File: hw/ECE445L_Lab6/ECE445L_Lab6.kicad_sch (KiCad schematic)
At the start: 32 parts, among them J1 JTAG, J2 Battery, SW1 Reset, SW2 Input, U1 TM4C123GH6PMIR, U2 Adafruit ST7735R, U3 LP2950-33LPRE3, Y1 ABM3-16.000MHZ-B2-T

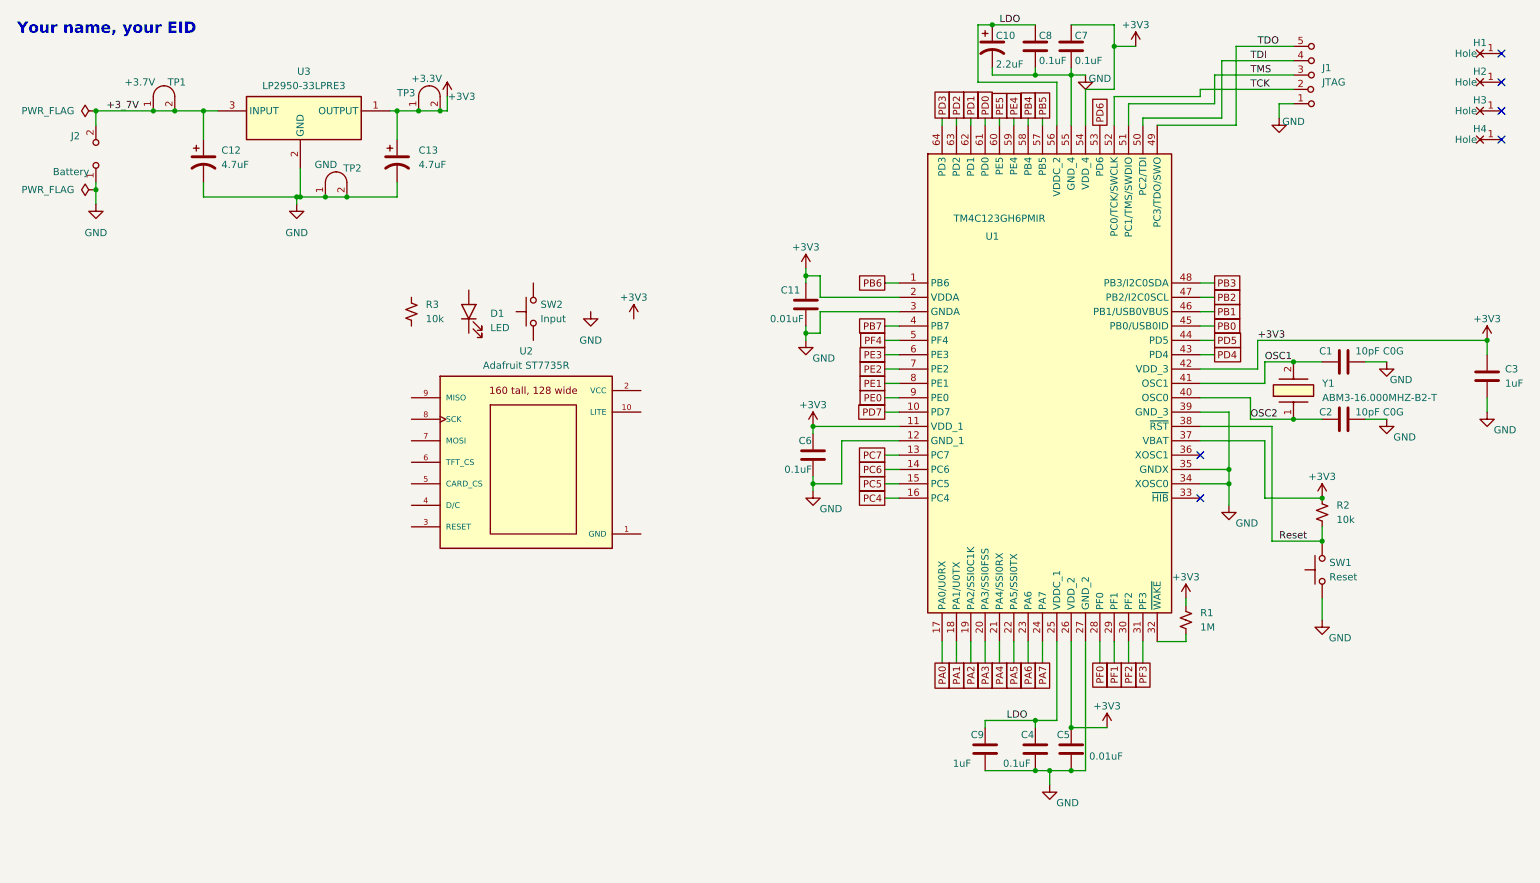
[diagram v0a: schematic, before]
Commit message: all hardware changes
fully updated schematic and pcb, most of changes were local to prevent corrupting files when pulling.
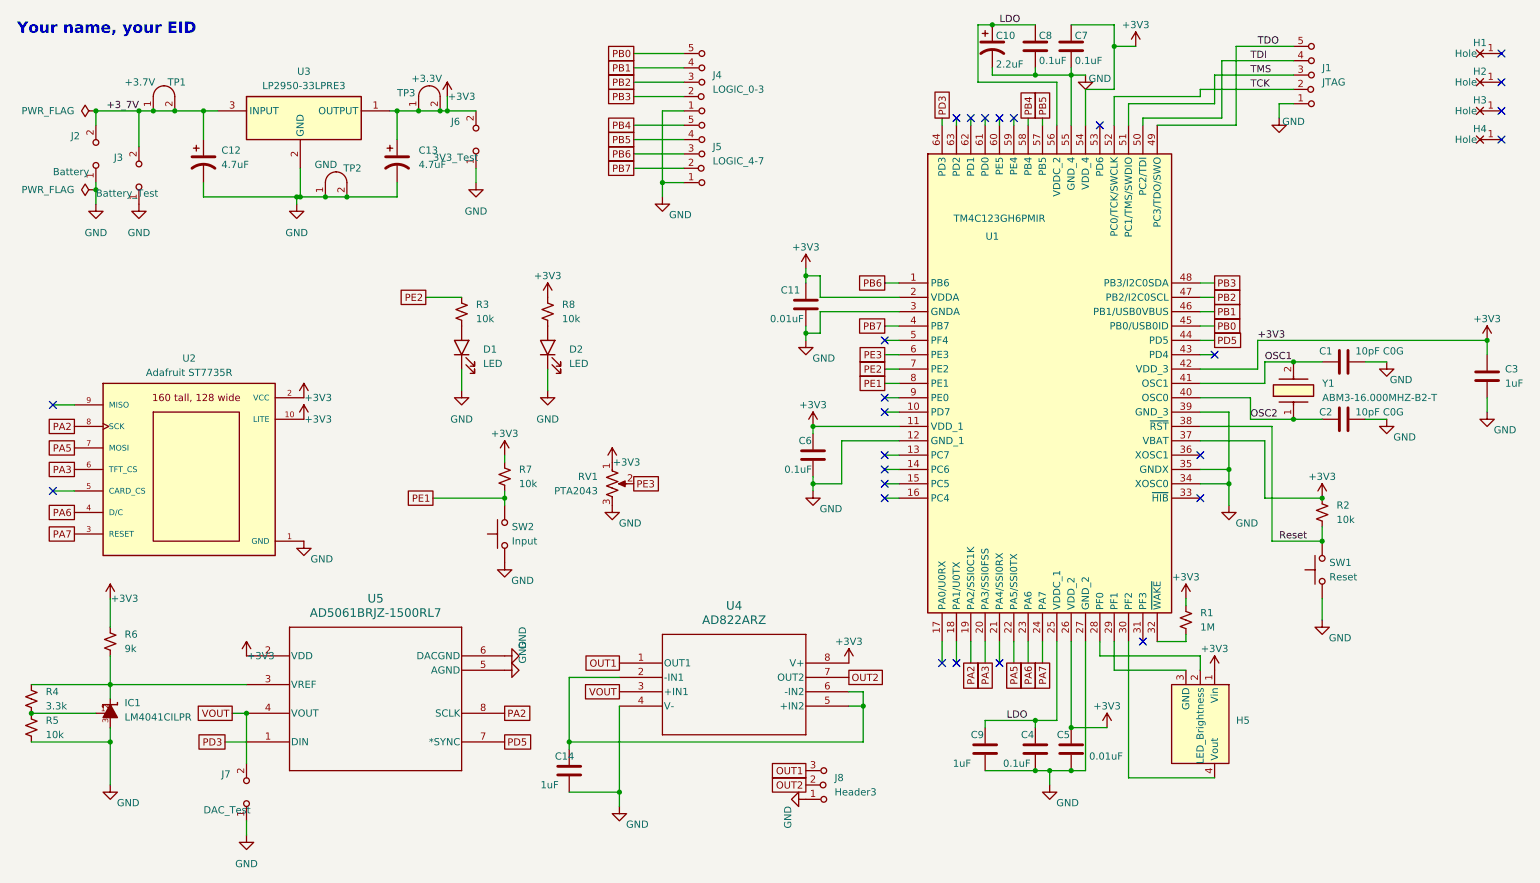
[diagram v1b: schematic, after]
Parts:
- added C14: 1uF, ECE445L:C_Axial_200mil, symbol ECE445L:C
- added D2: LED, ECE445L:LED_D5.0mm, symbol ECE445L:LED
- added H5: ~, Lab_6:HEARTBEAT, symbol lab6:heartbeat
- added IC1: LM4041CILPR, ECE445L:ti_LM4041CILPR, symbol ECE445L:LM4041CILPR
- added J3: Battery_Test, ECE445L:PinHeader_1x02_P2.54mm_Vertical, symbol ECE445L:Header_2
- added J4: LOGIC_0-3, ECE445L:PinHeader_1x05_P2.54mm_Vertical, symbol ECE445L:Header_5
- added J5: LOGIC_4-7, ECE445L:PinHeader_1x05_P2.54mm_Vertical, symbol ECE445L:Header_5
- added J6: 3V3_Test, ECE445L:PinHeader_1x02_P2.54mm_Vertical, symbol ECE445L:Header_2
- added J7: DAC_Test, ECE445L:PinHeader_1x02_P2.54mm_Vertical, symbol ECE445L:Header_2
- added J8: Header3, ECE445L:PinHeader_1x03_P2.54mm_Vertical, symbol ECE445L:Header_3
- added R4: 3.3k, ECE445L:R_Axial_DIN0204_L3.6mm_D1.6mm_P7.62mm_Horizontal, symbol ECE445L:R_0.125W
- added R5, R7, R8: 10k, ECE445L:R_Axial_DIN0204_L3.6mm_D1.6mm_P7.62mm_Horizontal, symbol ECE445L:R_0.125W
- added R6: 9k, ECE445L:R_Axial_DIN0204_L3.6mm_D1.6mm_P7.62mm_Horizontal, symbol ECE445L:R_0.125W
- added RV1: PTA2043, ECE445L:PTA2043pot, symbol ECE445L:PTA2043pot
- added U4: AD822ARZ, Lab_6:R_8_ADI, symbol AD822ARZ:AD822ARZ
- added U5: AD5061BRJZ-1500RL7, Lab_6:RJ_8_ADI, symbol AD5061BRJZ_1500RL7:AD5061BRJZ-1500RL7
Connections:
- net +3V3: now also U2.10 (LITE), U2.2 (VCC), H5.1 (Vin), J6.2 (B), R6.1, R7.1, R8.1, RV1.1, U4.8 (V+), U5.2 (VDD)
- net +3_7V: now also J3.2 (B)
- net GND: now also D1.1 (K), SW2.1, U2.1 (GND), C14.2, D2.1 (K), IC1.3, J3.1 (A), J4.1 (A), J5.1 (A), J6.1 (A), J7.1 (A), J8.1 (A), R5.2, RV1.3, U4.4 (V-), U5.5 (AGND), U5.6 (DACGND)
- net PA2: now also U2.8 (SCK), U5.8 (SCLK)
- net PA3: now also U2.6 (TFT_CS)
- net PA5: now also U2.7 (MOSI)
- net PA6: now also U2.4 (D/C)
- net PA7: now also U2.3 (RESET)
- net PB0: now also J4.5 (C)
- net PB1: now also J4.4 (C)
- net PB2: now also J4.3 (C)
- net PB3: now also J4.2 (B)
- net PB4: now also J5.5 (C)
- net PB5: now also J5.4 (C)
- net PB6: now also J5.3 (C)
- net PB7: now also J5.2 (B)
- net PD3: now also U5.1 (DIN)
- net PD5: now also U5.7 (*SYNC)
- net PE1: now also SW2.2, R7.2
- net PE2: now also R3.1
- net PE3: now also RV1.2
- net at D1.2 (A): now also R3.2
- net PA0: no longer names the net of U1.17 (PA0/U0RX)
- net PA1: no longer names the net of U1.18 (PA1/U0TX)
- net PA4: no longer names the net of U1.21 (PA4/SSI0RX)
- net PC4: no longer names the net of U1.16 (PC4)
- net PC5: no longer names the net of U1.15 (PC5)
- net PC6: no longer names the net of U1.14 (PC6)
- net PC7: no longer names the net of U1.13 (PC7)
- net PD0: no longer names the net of U1.61 (PD0)
- net PD1: no longer names the net of U1.62 (PD1)
- net PD2: no longer names the net of U1.63 (PD2)
- net PD4: no longer names the net of U1.43 (PD4)
- net PD6: no longer names the net of U1.53 (PD6)
- net PD7: no longer names the net of U1.10 (PD7)
- net PE0: no longer names the net of U1.9 (PE0)
- net PE4: no longer names the net of U1.59 (PE4)
- net PE5: no longer names the net of U1.60 (PE5)
- net PF0: no longer names the net of U1.28 (PF0)
- net PF0: now also H5.2 (LED_Brightness)
- net PF1: no longer names the net of U1.29 (PF1)
- net PF1: now also H5.3 (GND)
- net PF2: no longer names the net of U1.30 (PF2)
- net PF2: now also H5.4 (Vout)
- net PF3: no longer names the net of U1.31 (PF3)
- net PF4: no longer names the net of U1.5 (PF4)
- new net: C14.1, U4.2 (-IN1), U4.5 (+IN2), U4.6 (-IN2)
- new net: D2.2 (A), R8.2
- new net: IC1.2, R4.1, R6.2, U5.3 (VREF)
- new net: IC1.1, R4.2, R5.1
- new net OUT1: J8.3 (C), U4.1 (OUT1)
- new net OUT2: J8.2 (B), U4.7 (OUT2)
- new net VOUT: J7.2 (B), U4.3 (+IN1), U5.4 (VOUT)
- no-connect marks 6 -> 26
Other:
- moved on the sheet: D1, R3, SW2, U2
